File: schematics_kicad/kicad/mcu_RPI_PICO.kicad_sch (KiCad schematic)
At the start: 0 parts

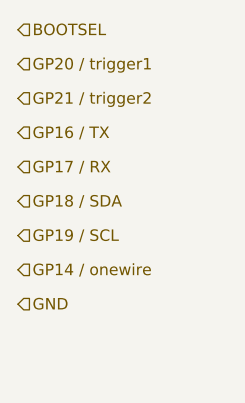
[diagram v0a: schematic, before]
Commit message: FUT_UART_LOOPBACK: LOLIN_D1_MINI, LOLIN_C3_MINI
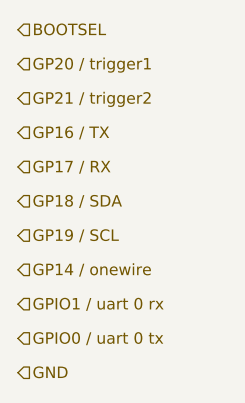
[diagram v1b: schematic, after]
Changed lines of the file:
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@@
 		(comment 1 "The MIT License (MIT)")
+	)
+	(hierarchical_label "GPIO1 {slash} uart 0 rx"
+		(shape input)
+		(at 82.55 91.44 0)
+		(fields_autoplaced yes)
+		(effects
+			(font
+				(size 1.27 1.27)
+			)
+			(justify left)
+		)
 	)
 	(hierarchical_label "GND"
 		(shape input)
-		(at 82.55 91.44 0)
+		(at 82.55 99.06 0)
 		(fields_autoplaced yes)
 		(effects
@@
 		(fields_autoplaced yes)
 		(effects
+			(font
+				(size 1.27 1.27)
+			)
+			(justify left)
+		)
+	)
+	(hierarchical_label "GPIO0 {slash} uart 0 tx"
+		(shape input)
+		(at 82.55 95.25 0)
+		(fields_autoplaced yes)
+		(effects
